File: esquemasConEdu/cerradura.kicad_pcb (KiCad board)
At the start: 2 copper layers, 85.8 x 137 mm, 16 parts, among them Q1 PN2222A

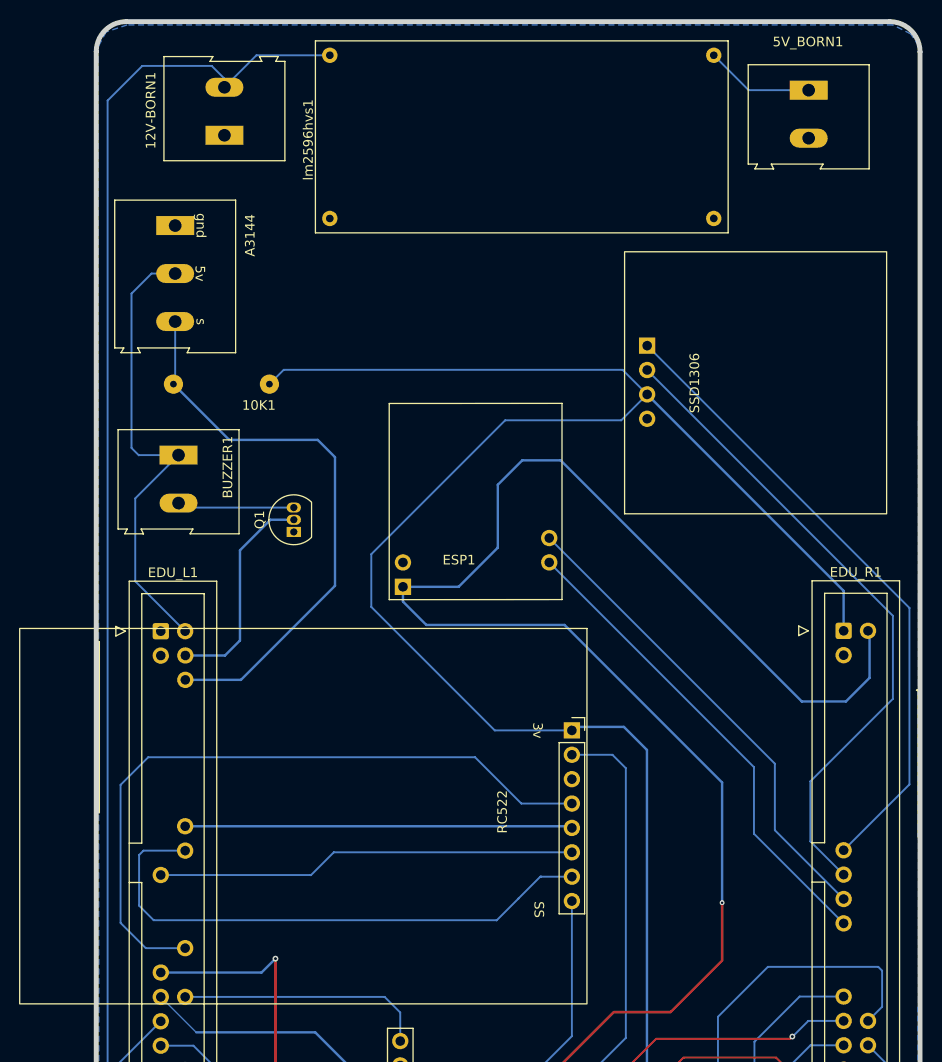
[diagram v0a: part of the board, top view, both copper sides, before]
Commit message: ajuste 3d, texto impreso
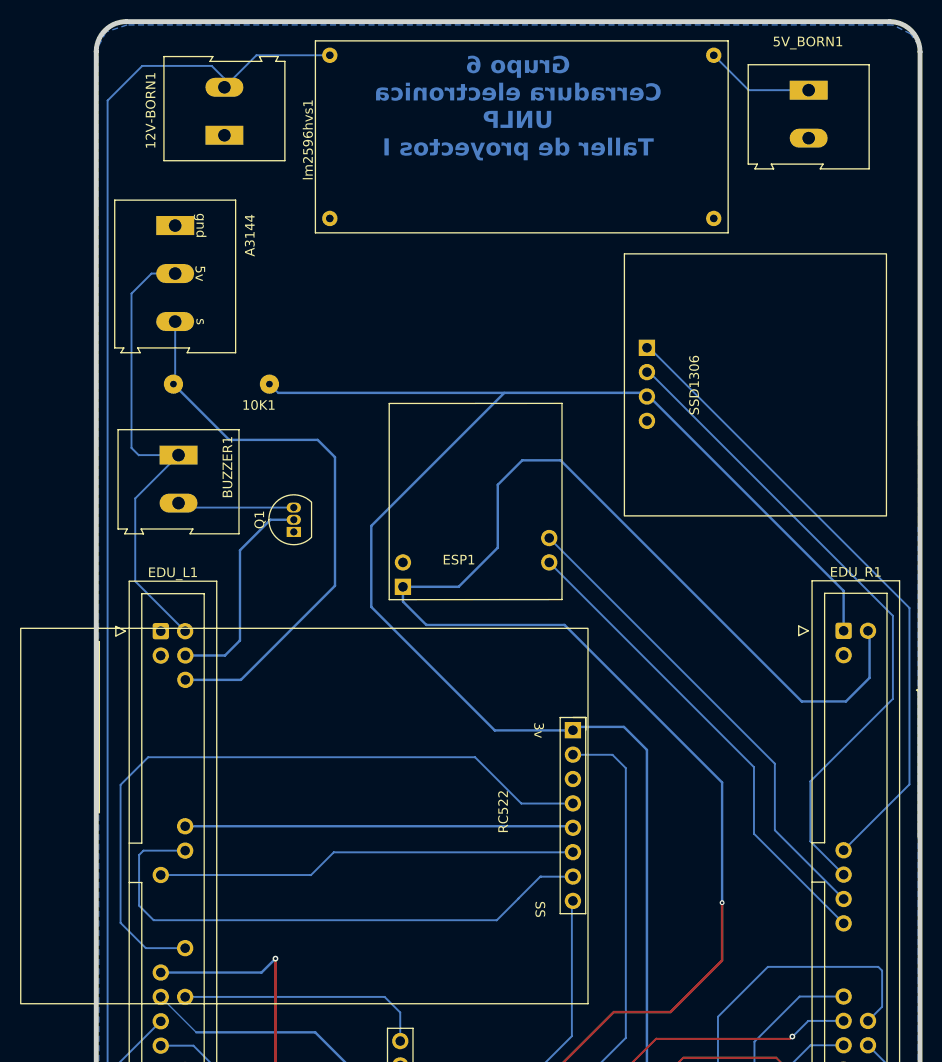
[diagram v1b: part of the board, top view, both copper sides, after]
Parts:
- moved RC522 16.1 mm to (95.1, 139.8), turned to 180 degrees
- moved SSD1306 11.9 mm to (102.8, 82.2), turned to 0 degrees
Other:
- board text added: "Grupo 6 Cerradura electronica UNLP Taller de proyectos I"

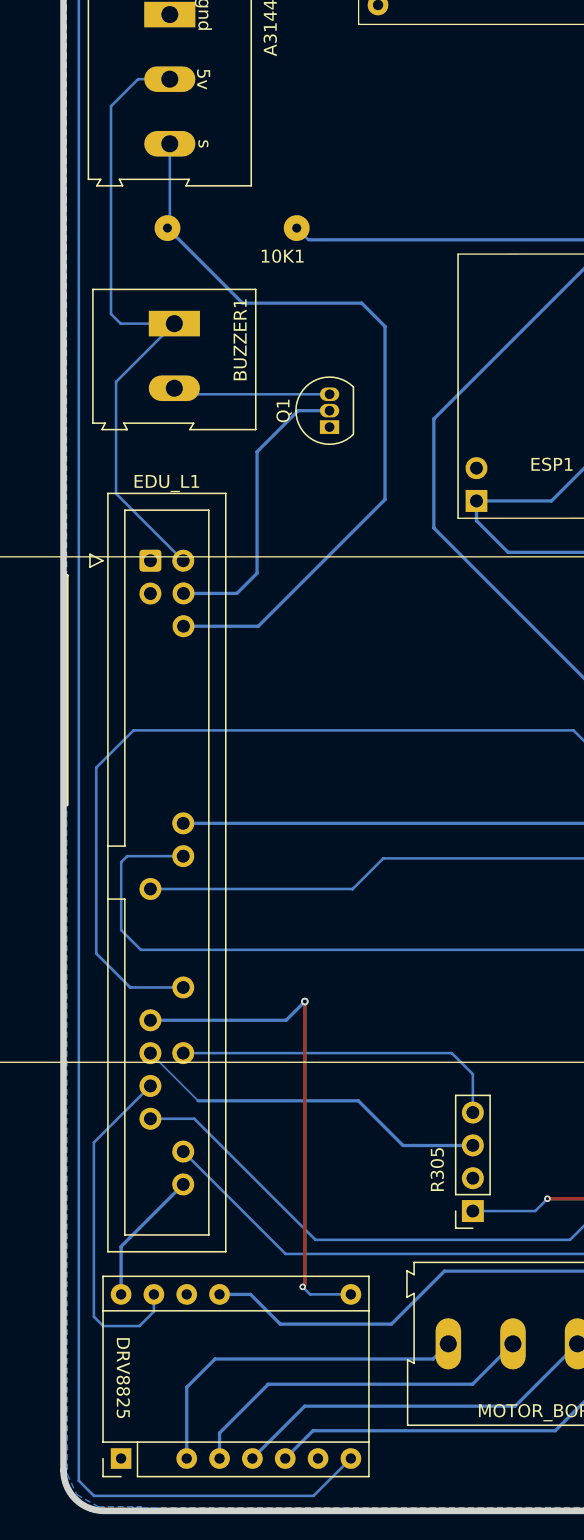
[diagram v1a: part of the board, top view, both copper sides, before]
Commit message: DRC corrido, marca algunos errores de conexion a tierra que deberian estar bien conectados
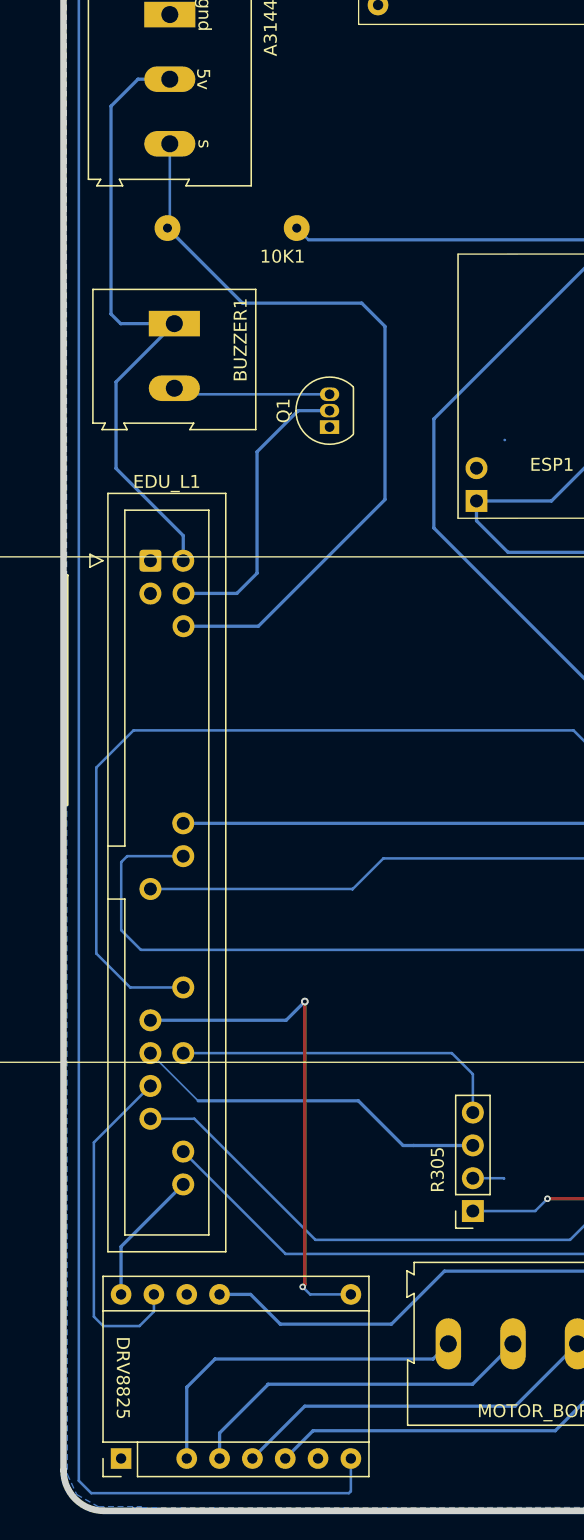
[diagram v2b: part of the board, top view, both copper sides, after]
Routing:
- net GND: track 0.00 -> 2.46 mm
- net +12V: track 176.7 -> 178.0 mm
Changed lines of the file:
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@@
 	)
 	(segment
-		(start 64.77 184.09)
-		(end 47.78 184.09)
+		(start 67.66 183.73)
+		(end 67.51 183.88)
+		(width 0.2)
+		(layer "B.Cu")
+		(net 3)
+	)
+	(segment
+		(start 67.66 181.2)
+		(end 67.66 183.73)
+		(width 0.2)
+		(layer "B.Cu")
+		(net 3)
+	)
+	(segment
+		(start 47.57 183.88)
+		(end 46.61 182.92)
+		(width 0.2)
+		(layer "B.Cu")
+		(net 3)
+	)
+	(segment
+		(start 58.78 54.16)
+		(end 58.78 55.065)
+		(width 0.2)
+		(layer "B.Cu")
+		(net 3)
+	)
+	(segment
+		(start 50.22 52.84)
+		(end 57.46 52.84)
+		(width 0.2)
+		(layer "B.Cu")
+		(net 3)
+	)
+	(segment
+		(start 46.61 182.92)
+		(end 46.61 56.45)
+		(width 0.2)
+		(layer "B.Cu")
+		(net 3)
+	)
+	(segment
+		(start 69.76 51.73)
+		(end 62.115 51.73)
+		(width 0.2)
+		(layer "B.Cu")
+		(net 3)
+	)
+	(segment
+		(start 67.51 183.88)
+		(end 47.57 183.88)
 		(width 0.2)
 		(layer "B.Cu")
@@
 	)
 	(segment
+		(start 62.115 51.73)
+		(end 58.78 55.065)
+		(width 0.2)
+		(layer "B.Cu")
+		(net 3)
+	)
+	(segment
 		(start 46.61 56.45)
 		(end 50.22 52.84)
-		(width 0.2)
-		(layer "B.Cu")
-		(net 3)
-	)
-	(segment
-		(start 67.66 181.2)
-		(end 64.77 184.09)
-		(width 0.2)
-		(layer "B.Cu")
-		(net 3)
-	)
-	(segment
-		(start 46.61 182.92)
-		(end 46.61 56.45)
-		(width 0.2)
-		(layer "B.Cu")
-		(net 3)
-	)
-	(segment
-		(start 50.22 52.84)
-		(end 57.46 52.84)
-		(width 0.2)
-		(layer "B.Cu")
-		(net 3)
-	)
-	(segment
-		(start 69.76 51.73)
-		(end 62.115 51.73)
-		(width 0.2)
-		(layer "B.Cu")
-		(net 3)
-	)
-	(segment
-		(start 47.78 184.09)
-		(end 46.61 182.92)
-		(width 0.2)
-		(layer "B.Cu")
-		(net 3)
-	)
-	(segment
-		(start 58.78 54.16)
-		(end 58.78 55.065)
-		(width 0.2)
-		(layer "B.Cu")
-		(net 3)
-	)
-	(segment
-		(start 62.115 51.73)
-		(end 58.78 55.065)
 		(width 0.2)
 		(layer "B.Cu")
@@
 		(start 49.1 92.64)
 		(end 49.86 93.4)
-		(width 0.2)
+		(width 0.254)
+		(layer "B.Cu")
+		(net 4)
+	)
+	(segment
+		(start 49.49 97.895)
+		(end 49.49 104.59)
+		(width 0.254)
+		(layer "B.Cu")
+		(net 4)
+	)
+	(segment
+		(start 87.26 103.03)
+		(end 87.26 96.48)
+		(width 0.254)
+		(layer "B.Cu")
+		(net 4)
+	)
+	(segment
+		(start 82.87 161.1)
+		(end 81.92 162.05)
+		(width 0.2)
+		(layer "B.Cu")
+		(net 4)
+	)
+	(segment
+		(start 110.63 127.49)
+		(end 94.22 111.08)
+		(width 0.254)
+		(layer "B.Cu")
+		(net 4)
+	)
+	(segment
+		(start 51.19 74.47)
+		(end 49.1 76.56)
+		(width 0.254)
+		(layer "B.Cu")
+		(net 4)
+	)
+	(segment
+		(start 123.53 119.05)
+		(end 125.99 116.59)
+		(width 0.254)
+		(layer "B.Cu")
+		(net 4)
+	)
+	(segment
+		(start 53.65 74.47)
+		(end 51.19 74.47)
+		(width 0.254)
+		(layer "B.Cu")
+		(net 4)
+	)
+	(segment
+		(start 83.185 107.105)
+		(end 87.26 103.03)
+		(width 0.254)
+		(layer "B.Cu")
+		(net 4)
+	)
+	(segment
+		(start 87.26 96.48)
+		(end 89.81 93.93)
+		(width 0.254)
+		(layer "B.Cu")
+		(net 4)
+	)
+	(segment
+		(start 79.82 111.08)
+		(end 77.38 108.64)
+		(width 0.254)
+		(layer "B.Cu")
+		(net 4)
+	)
+	(segment
+		(start 81.92 162.05)
+		(end 77.1 162.05)
+		(width 0.2)
+		(layer "B.Cu")
+		(net 4)
+	)
+	(segment
+		(start 49.875 93.385)
+		(end 54 93.385)
+		(width 0.254)
+		(layer "B.Cu")
+		(net 4)
+	)
+	(segment
+		(start 110.63 140.02)
+		(end 110.63 127.49)
+		(width 0.254)
+		(layer "B.Cu")
+		(net 4)
+	)
+	(segment
+		(start 77.38 108.64)
+		(end 77.38 107.105)
+		(width 0.254)
+		(layer "B.Cu")
+		(net 4)
+	)
+	(segment
+		(start 89.81 93.93)
+		(end 93.81 93.93)
+		(width 0.254)
 		(layer "B.Cu")
 		(net 4)
@@
 		(start 54 93.385)
 		(end 49.49 97.895)
-		(width 0.2)
-		(layer "B.Cu")
-		(net 4)
-	)
-	(segment
-		(start 87.26 103.03)
-		(end 87.26 96.48)
-		(width 0.254)
-		(layer "B.Cu")
-		(net 4)
-	)
-	(segment
-		(start 82.87 161.1)
-		(end 81.92 162.05)
-		(width 0.2)
-		(layer "B.Cu")
-		(net 4)
-	)
-	(segment
-		(start 110.63 127.49)
-		(end 94.22 111.08)
-		(width 0.254)
-		(layer "B.Cu")
-		(net 4)
-	)
-	(segment
-		(start 51.19 74.47)
-		(end 49.1 76.56)
-		(width 0.2)
-		(layer "B.Cu")
-		(net 4)
-	)
-	(segment
-		(start 123.53 119.05)
-		(end 125.99 116.59)
-		(width 0.254)
-		(layer "B.Cu")
-		(net 4)
-	)
-	(segment
-		(start 53.65 74.47)
-		(end 51.19 74.47)
-		(width 0.2)
-		(layer "B.Cu")
-		(net 4)
-	)
-	(segment
-		(start 83.185 107.105)
-		(end 87.26 103.03)
-		(width 0.254)
-		(layer "B.Cu")
-		(net 4)
-	)
-	(segment
-		(start 87.26 96.48)
-		(end 89.81 93.93)
-		(width 0.254)
-		(layer "B.Cu")
-		(net 4)
-	)
-	(segment
-		(start 79.82 111.08)
-		(end 77.38 108.64)
-		(width 0.254)
-		(layer "B.Cu")
-		(net 4)
-	)
-	(segment
-		(start 81.92 162.05)
-		(end 77.1 162.05)
-		(width 0.2)
-		(layer "B.Cu")
-		(net 4)
-	)
-	(segment
-		(start 49.875 93.385)
-		(end 54 93.385)
-		(width 0.2)
-		(layer "B.Cu")
-		(net 4)
-	)
-	(segment
-		(start 110.63 140.02)
-		(end 110.63 127.49)
-		(width 0.254)
-		(layer "B.Cu")
-		(net 4)
-	)
-	(segment
-		(start 77.38 108.64)
-		(end 77.38 107.105)
-		(width 0.254)
-		(layer "B.Cu")
-		(net 4)
-	)
-	(segment
-		(start 89.81 93.93)
-		(end 93.81 93.93)
 		(width 0.254)
 		(layer "B.Cu")
@@
 	)
 	(segment
+		(start 54.69 109.79)
+		(end 54.69 111.73)
+		(width 0.254)
+		(layer "B.Cu")
+		(net 4)
+	)
+	(segment
 		(start 93.81 93.93)
 		(end 118.93 119.05)
@@
 	)
 	(segment
-		(start 49.49 106.53)
-		(end 54.69 111.73)
-		(width 0.2)
+		(start 49.49 104.59)
+		(end 54.69 109.79)
+		(width 0.254)
 		(layer "B.Cu")
 		(net 4)
@@
 		(start 49.1 76.56)
 		(end 49.1 92.64)
-		(width 0.2)
-		(layer "B.Cu")
-		(net 4)
-	)
-	(segment
-		(start 49.49 97.895)
-		(end 49.49 106.53)
-		(width 0.2)
+		(width 0.254)
 		(layer "B.Cu")
 		(net 4)
@@
 	)
 	(segment
+		(start 79.555 102.39)
+		(end 79.58 102.39)
+		(width 0.2)
+		(layer "B.Cu")
+		(net 5)
+	)
+	(segment
+		(start 79.49 159.51)
+		(end 79.52 159.54)
+		(width 0.2)
+		(layer "B.Cu")
+		(net 5)
+	)
+	(segment
+		(start 77.1 159.51)
+		(end 79.49 159.51)
+		(width 0.2)
+		(layer "B.Cu")
+		(net 5)
+	)
+	(segment

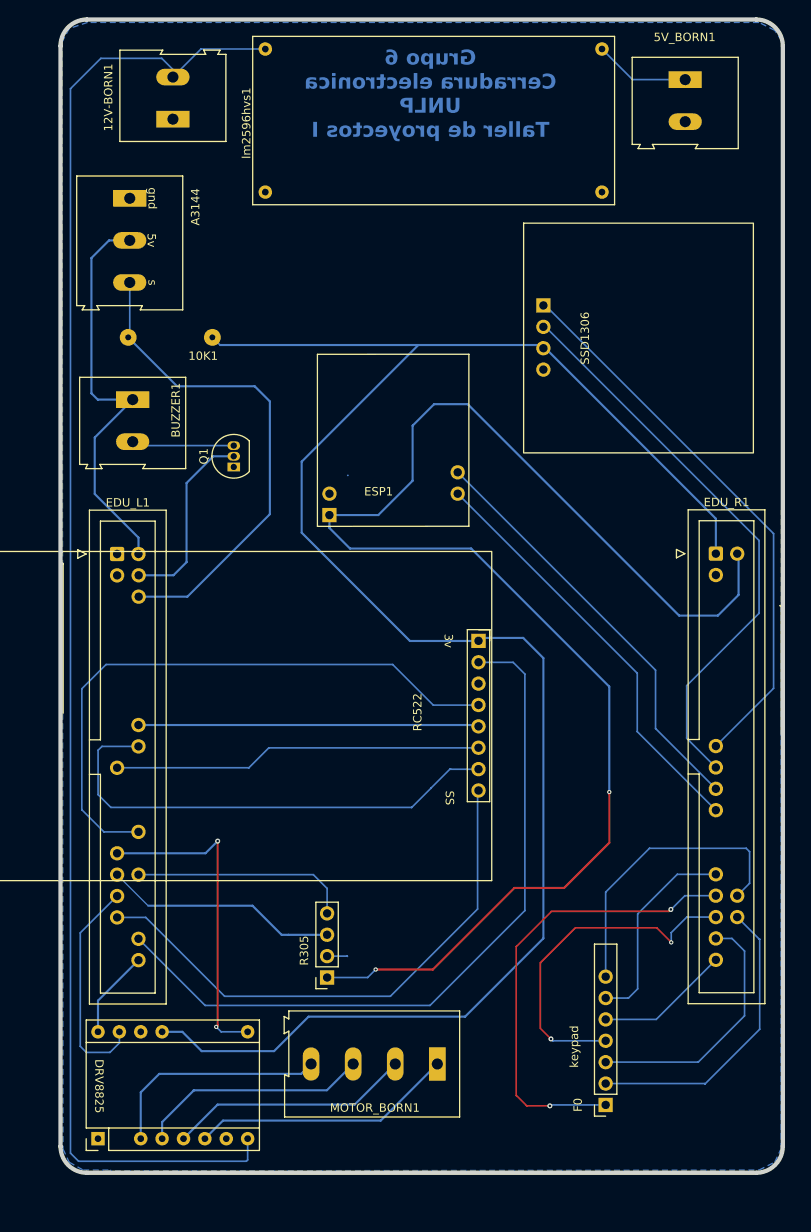
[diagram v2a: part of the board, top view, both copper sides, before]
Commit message: fix ancho pistas 1mm
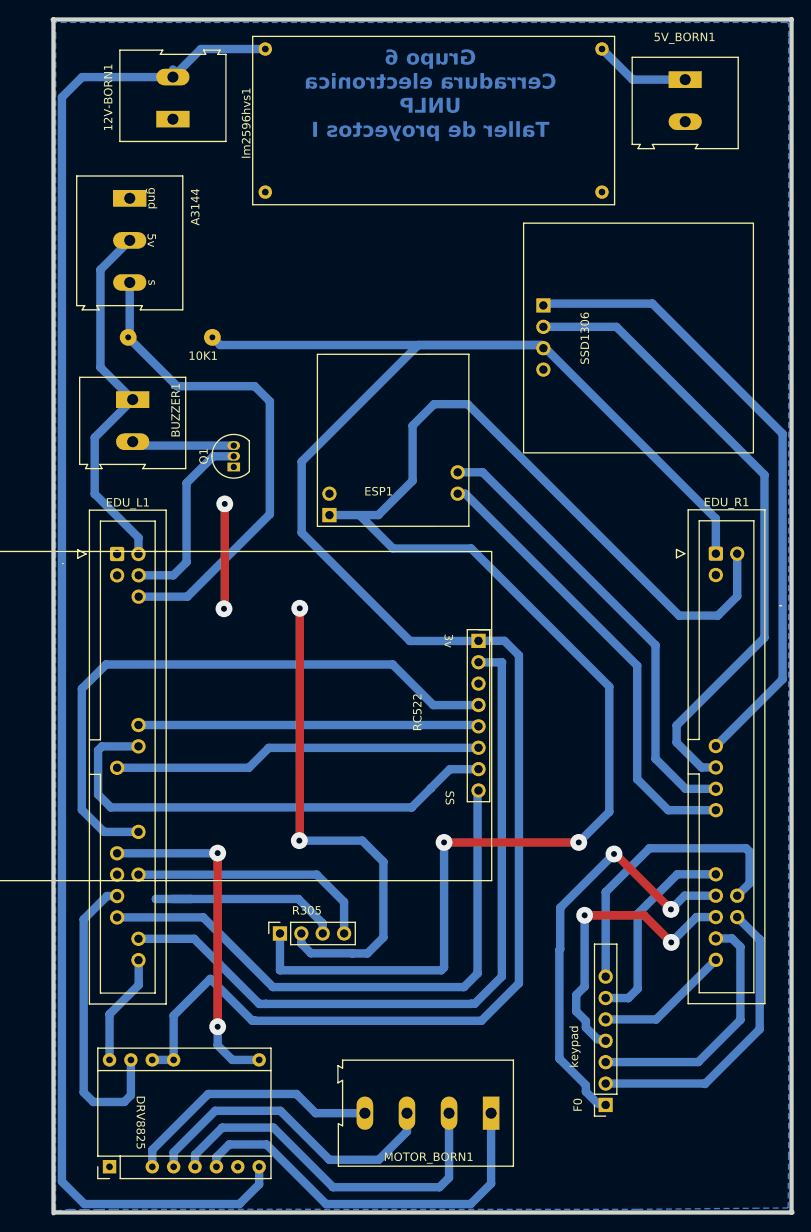
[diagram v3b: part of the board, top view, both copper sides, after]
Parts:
- moved MOTOR_BORN1 8.66 mm to (96.6, 178.2)
- moved R305 7.66 mm to (71.5, 156.8), turned to 90 degrees
- moved DRV8825 3.61 mm to (51.2, 184.5)
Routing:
- net GND: track 2.46 -> 72.7 mm, vias 0 -> 4
- net /drv882x_b2: track 31.3 -> 46.7 mm
- net /drv882x_b1: track 28.8 -> 44.0 mm
- net /drv882x_a1: track 27.5 -> 37.5 mm
- net /drv882x_step: track 26.4 -> 36.3 mm
- net /ssd1306_sda: track 66.7 -> 75.2 mm
- net /ssd1306_scl: track 68.2 -> 75.6 mm
- net +5V: track 224.7 -> 231.5 mm
- net /kp_f3: track 41.4 -> 35.4 mm
- net +12V: track 178.0 -> 183.9 mm
- net +3.3V: track 236.0 -> 241.4 mm
- net /kp_f0: track 55.1 -> 51.1 mm
- net /esp32_tx: track 50.3 -> 54.2 mm
- net /esp32_rx: track 50.3 -> 54.1 mm
- net /drv882x_a2: track 27.1 -> 31.0 mm
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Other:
- board size 85.8 x 137 mm -> 87.9 x 141.9 mm

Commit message: 'Todo' conectado 1 mm
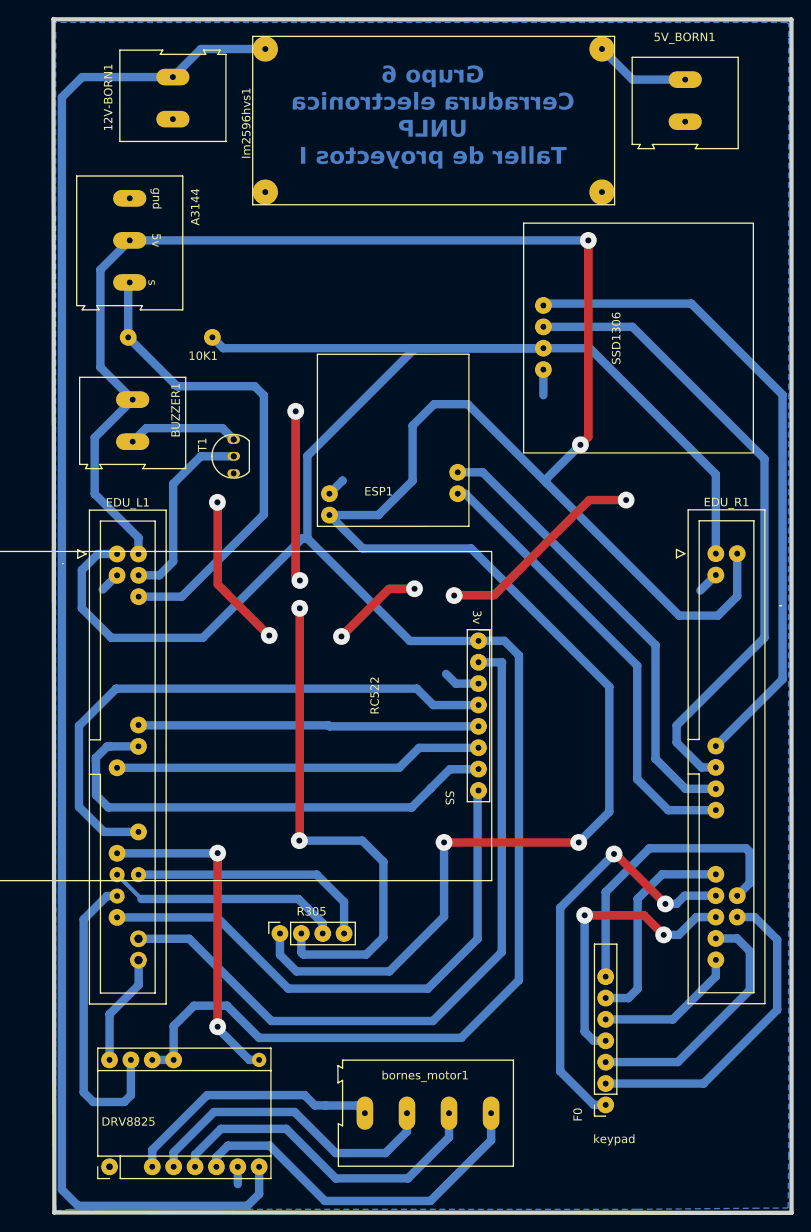
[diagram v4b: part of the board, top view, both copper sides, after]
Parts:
- A3144: value Bornera Sensor Hall -> A3144
- EDU_L1: value EDU_CIAA_LEFT_SOCKET -> EDU_L
- EDU_R1: value EDU_CIAA_RIGHT_SOCKET -> EDU_R
- ESP1: value ESP32_SOCKET -> ESP
- RC522: value RC522_sensor -> RC522
- T1: renamed from Q1; value PN2222A -> BC547
- renumbered MOTOR_BORN1 to bornes_motor1, Keypad1 to num_keypad1
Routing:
- net +5V: track 231.5 -> 315.9 mm, vias 2 -> 4
- net GND: track 72.7 -> 152.1 mm, vias 4 -> 10
- net +3.3V: track 241.4 -> 284.7 mm
- net /rc522-irq: track 72.4 -> 67.9 mm
- net /drv882x_b1: track 44.0 -> 40.2 mm
- net /r305_tx: track 24.5 -> 28.0 mm
- net /drv882x_b2: track 46.7 -> 43.3 mm
- net /kp_f1: track 35.5 -> 38.2 mm
- net /ssd1306_sda: track 75.2 -> 77.9 mm
- net /rc522-ss: track 68.7 -> 66.4 mm
- net /kp_f3: track 35.4 -> 34.2 mm
- net /drv882x_en: track 40.4 -> 39.3 mm
- net /kp_c0: track 16.0 -> 17.2 mm
- net /ssd1306_scl: track 75.6 -> 76.7 mm
- net /kp_c1: track 24.4 -> 25.5 mm
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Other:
- board size 87.9 x 141.9 mm -> 87.7 x 141.8 mm

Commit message: no deberia tener cambios este commit
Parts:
- moved 5V_BORN1 139.8 mm to (256.4, 26.4)
- moved RC522 139.8 mm to (231.9, 110.9)
- moved 10K1 139.8 mm to (199.2, 57.0)
- moved 12V-BORN1 139.8 mm to (195.5, 31.1)
- moved A3144 139.8 mm to (190.4, 40.5)
- moved BUZZER1 139.8 mm to (190.8, 64.4)
- moved DRV8825 139.8 mm to (188.0, 155.6)
- moved EDU_L1 139.8 mm to (188.9, 82.8)
- moved EDU_R1 139.8 mm to (260.1, 82.7)
- moved ESP1 139.8 mm to (226.8, 78.1)
- moved R305 139.8 mm to (208.3, 127.8)
- moved SSD1306 139.8 mm to (239.6, 53.2)
- moved T1 139.8 mm to (202.8, 72.4)
- moved bornes_motor1 139.8 mm to (233.4, 149.2)
- moved lm2596hvs1 139.8 mm to (226.5, 30.3)
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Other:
- board text added: "0.0.1"
- board text added: "3/11/2025"
- board text added: "Cerradura electronica Grupo 6 Taller de proyectos I UNLP"
